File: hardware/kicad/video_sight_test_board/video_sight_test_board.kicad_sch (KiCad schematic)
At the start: 50 parts, among them J1 BATTERY, J2 XIAO_BREAKOUT_BOARD, J3 LCD, J4 BNO055_MODULE, J4 Conn_01x03_Pin, J5 ATtiny1616_LEFT, J6 ATtiny1616_RIGHT, J7 INPUT_DEVICE, Q1 AO3401A, SW1 SW_BATT, SW2 SW_MEC_5G, SW3 SW_MEC_5G, SW4 SW_MEC_5G, SW5 SW_MEC_5G, SW6 RotaryEncoder, U2 TPS22919, U3 ATtiny1616-S

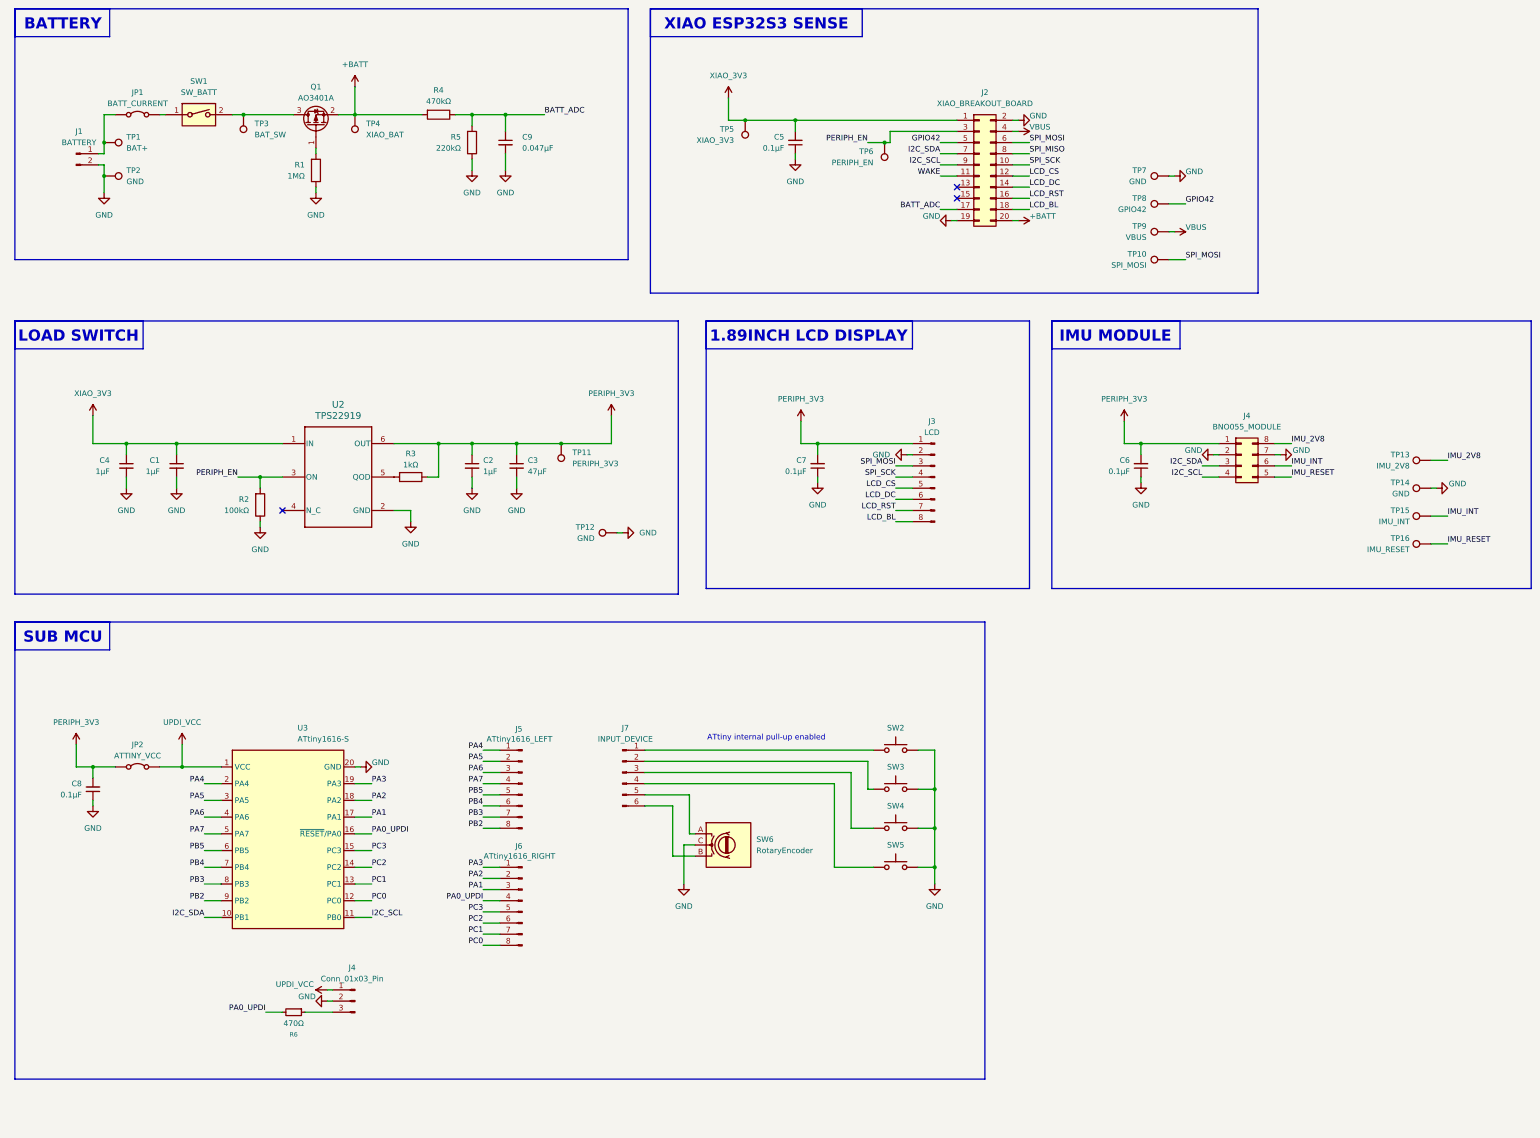
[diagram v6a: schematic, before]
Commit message: テストボード回路図修正 I2Cプルアップ追加 C8位置修正
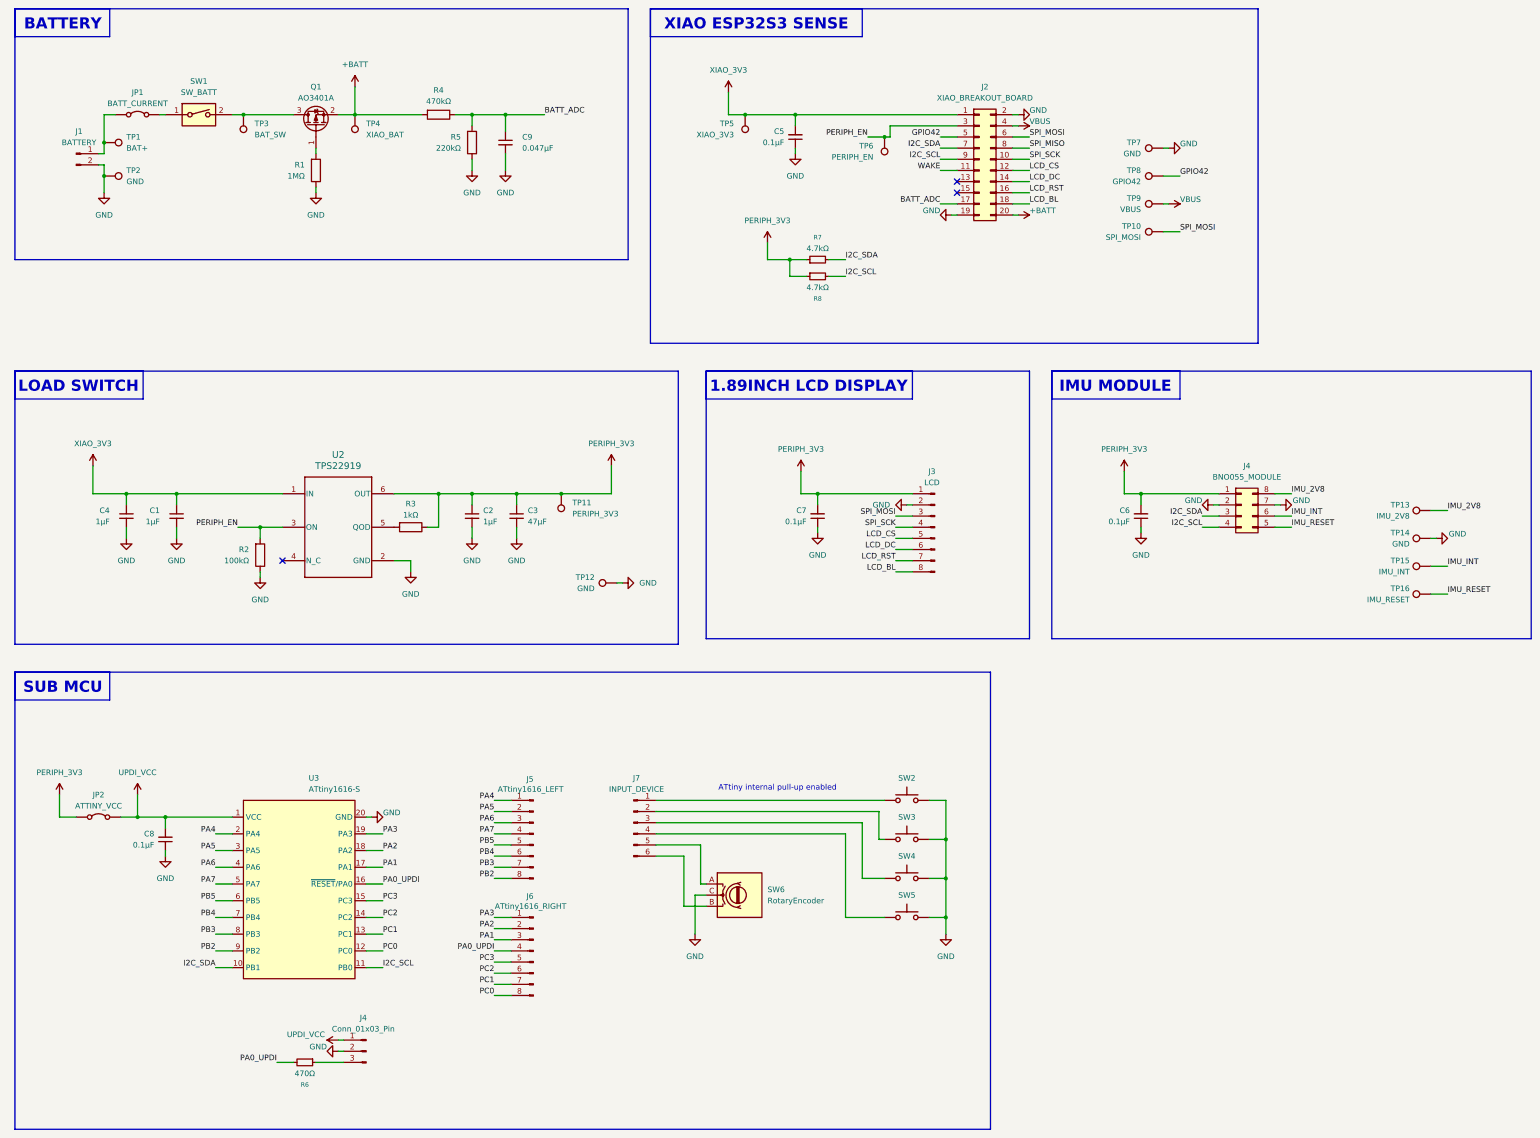
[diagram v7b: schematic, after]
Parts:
- added R7, R8: 4.7kΩ, symbol Device:R_Small
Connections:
- net I2C_SCL: now also R8.2
- net I2C_SDA: now also R7.2
- net PERIPH_3V3: now also R7.1, R8.1; no longer C8.2
- net UPDI_VCC: now also C8.2
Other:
- moved on the sheet: C1, C2, C3, C4, C5, C6, C7, C8, J2, J3, J4, J5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

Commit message: リファレンス修正
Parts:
- renumbered U2 to U1, U3 to U2
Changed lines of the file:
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@@
 		(dnp no)
 		(fields_autoplaced yes)
-		(property "Reference" "U2"
+		(property "Reference" "U1"
 			(at 90.17 118.11 0)
 			(effects
@@
 			(project ""
 				(path "/1bc004cb-e275-41d9-96ac-81dd92544364"
-					(reference "U2")
+					(reference "U1")
 					(unit 1)
 				)
@@
 		(dnp no)
 		(fields_autoplaced yes)
-		(property "Reference" "U3"
-			(at 83.4233 191.77 0)
-			(effects
-				(font
-					(size 1.27 1.27)
-				)
-				(justify left)
+		(property "Reference" "U2"
+			(at 81.28 191.77 0)
+			(effects
+				(font
+					(size 1.27 1.27)
+				)
 			)
 		)
 		(property "Value" "ATtiny1616-S"
-			(at 83.4233 194.31 0)
-			(effects
-				(font
-					(size 1.27 1.27)
-				)
-				(justify left)
+			(at 81.28 194.31 0)
+			(effects
+				(font
+					(size 1.27 1.27)
+				)
 			)
 		)
@@
 			(project ""
 				(path "/1bc004cb-e275-41d9-96ac-81dd92544364"
-					(reference "U3")
-					(unit 1)
-				)
+					(reference "U2")
+					(unit 1)
+				)
